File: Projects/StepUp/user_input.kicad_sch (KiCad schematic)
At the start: 1 part, among them U6 COM-09032

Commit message: feat(charge): Charge IC, USB ESD, sheet sections
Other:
- moved on the sheet: U6
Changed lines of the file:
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@@
 	(symbol
 		(lib_id "COM-09032:COM-09032")
-		(at 115.57 130.81 0)
+		(at 200.66 137.16 0)
 		(unit 1)
 		(exclude_from_sim no)
@@
 		(fields_autoplaced yes)
 		(property "Reference" "U6"
-			(at 124.46 130.8099 0)
+			(at 209.55 137.1599 0)
 			(effects
 				(font
@@
 		)
 		(property "Value" "COM-09032"
-			(at 124.46 133.3499 0)
+			(at 209.55 139.6999 0)
 			(effects
 				(font
@@
 		)
 		(property "Footprint" "joystick_footprints:XDCR_COM-09032"
-			(at 115.57 130.81 0)
+			(at 200.66 137.16 0)
 			(effects
 				(font
@@
 		)
 		(property "Datasheet" ""
-			(at 115.57 130.81 0)
+			(at 200.66 137.16 0)
 			(effects
 				(font
@@
 		)
 		(property "Description" ""
-			(at 115.57 130.81 0)
+			(at 200.66 137.16 0)
 			(effects
 				(font
@@
 		)
 		(property "MF" "SparkFun Electronics"
-			(at 115.57 130.81 0)
+			(at 200.66 137.16 0)
 			(effects
 				(font
@@
 		)
 		(property "MAXIMUM_PACKAGE_HEIGHT" "30.1mm"
-			(at 115.57 130.81 0)
+			(at 200.66 137.16 0)
 			(effects
 				(font
@@
 		)
 		(property "Package" "Package"
-			(at 115.57 130.81 0)
+			(at 200.66 137.16 0)
 			(effects
 				(font
@@
 		)
 		(property "Price" "None"
-			(at 115.57 130.81 0)
+			(at 200.66 137.16 0)
 			(effects
 				(font
@@
 		)
 		(property "Check_prices" "https://www.snapeda.com/parts/COM-09032/SparkFun+Electronics/view-part/?ref=eda"
-			(at 115.57 130.81 0)
+			(at 200.66 137.16 0)
 			(effects
 				(font
@@
 		)
 		(property "STANDARD" "Manufacturer Recommendations"
-			(at 115.57 130.81 0)
+			(at 200.66 137.16 0)
 			(effects
 				(font
@@
 		)
 		(property "PARTREV" "N/A"
-			(at 115.57 130.81 0)
+			(at 200.66 137.16 0)
 			(effects
 				(font
@@
 		)
 		(property "SnapEDA_Link" "https://www.snapeda.com/parts/COM-09032/SparkFun+Electronics/view-part/?ref=snap"
-			(at 115.57 130.81 0)
+			(at 200.66 137.16 0)
 			(effects
 				(font
@@
 		)
 		(property "MP" "COM-09032"
-			(at 115.57 130.81 0)
+			(at 200.66 137.16 0)
 			(effects
 				(font
@@
 		)
 		(property "Purchase-URL" "https://www.snapeda.com/api/url_track_click_mouser/?unipart_id=888157&manufacturer=SparkFun Electronics&part_name=COM-09032&search_term=joystick"
-			(at 115.57 130.81 0)
+			(at 200.66 137.16 0)
 			(effects
 				(font
@@
 		)
 		(property "Description_1" "\nJoystick, 2 - Axis Analog (Resistive) Output\n"
-			(at 115.57 130.81 0)
+			(at 200.66 137.16 0)
 			(effects
 				(font
@@
 		)
 		(property "Availability" "In Stock"
-			(at 115.57 130.81 0)
+			(at 200.66 137.16 0)
 			(effects
 				(font
@@
 		)
 		(property "MANUFACTURER" "SparkFun Electronics"
-			(at 115.57 130.81 0)
+			(at 200.66 137.16 0)
 			(effects
 				(font

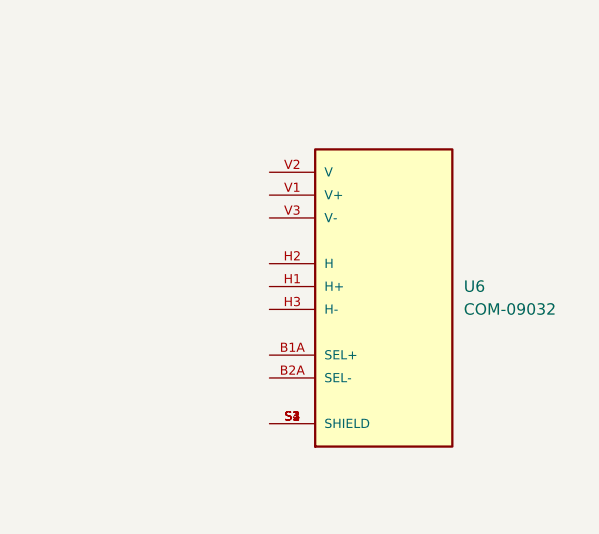
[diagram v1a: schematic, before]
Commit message: feat(power): Input stage updates
USB vs Vbat source selection using PMOS gate logic.
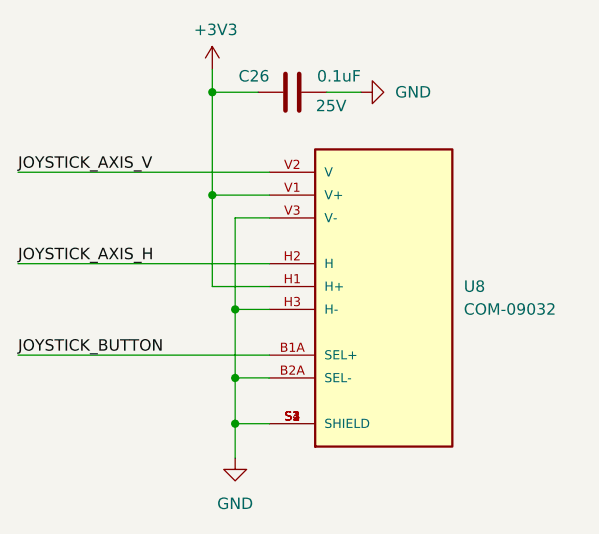
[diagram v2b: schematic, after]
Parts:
- added C26: 0.1uF, Capacitor_SMD:C_0603_1608Metric, symbol Device:C
- renumbered U6 to U8
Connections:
- net JOYSTICK_BUTTON: now reaches U8.B1A (SEL+)
- net GND: now reaches U8.B2A (SEL-)
- net GND: now also U8.H3 (H-), U8.S1 (SHIELD), U8.S2 (SHIELD), U8.S3 (SHIELD), U8.S4 (SHIELD), U8.V3 (V-), C26.2
- net +3V3: now reaches U8.H1 (H+)
- net +3V3: now also U8.V1 (V+), C26.1
- net JOYSTICK_AXIS_H: now reaches U8.H2 (H)
- net JOYSTICK_AXIS_V: now reaches U8.V2 (V)

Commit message: feat(stepup): Many additions
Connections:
- net JOYSTICK_AXIS_H renamed JOYSTSICK_AXIS_H
- net JOYSTICK_AXIS_V renamed JOYSTSICK_AXIS_V
- net JOYSTICK_BUTTON renamed JOYSTSICK_BUTTON
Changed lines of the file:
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@@
+		)
+	)
+	(global_label "JOYSTSICK_AXIS_H"
+		(shape input)
+		(at 160.02 134.62 180)
+		(fields_autoplaced yes)
+		(effects
+			(font
+				(size 1.27 1.27)
+				(color 255 255 194 1)
+			)
+			(justify right)
+		)
+		(property "Intersheetrefs" "${INTERSHEET_REFS}"
+			(at 139.7386 134.62 0)
+			(effects
+				(font
+					(size 1.27 1.27)
+				)
+				(justify right)
+				(hide yes)
+			)
+		)
+	)
+	(global_label "JOYSTSICK_AXIS_V"
+		(shape input)
+		(at 160.02 124.46 180)
+		(fields_autoplaced yes)
+		(effects
+			(font
+				(size 1.27 1.27)
+				(color 255 255 194 1)
+			)
+			(justify right)
+		)
+		(property "Intersheetrefs" "${INTERSHEET_REFS}"
+			(at 139.9805 124.46 0)
+			(effects
+				(font
+					(size 1.27 1.27)
+				)
+				(justify right)
+				(hide yes)
+			)
+		)
+	)
+	(global_label "JOYSTSICK_BUTTON"
+		(shape input)
+		(at 160.02 144.78 180)
+		(fields_autoplaced yes)
+		(effects
+			(font
+				(size 1.27 1.27)
+				(color 255 255 194 1)
+			)
+			(justify right)
+		)
+		(property "Intersheetrefs" "${INTERSHEET_REFS}"
+			(at 138.9524 144.78 0)
+			(effects
+				(font
+					(size 1.27 1.27)
+				)
+				(justify right)
+				(hide yes)
+			)
 		)
 	)
@@
 				(path "/e0cca1c7-c263-49eb-8c40-74000ebe5285/62dd6998-8b69-42c0-9c2f-b18953d44bc4"
 					(reference "C26")
+					(unit 1)
+				)
+				(path "/e0cca1c7-c263-49eb-8c40-74000ebe5285/b287fd2a-b2a9-45b4-81d1-0975d80d8cfc"
+					(reference "C28")
 					(unit 1)
 				)
@@
 					(unit 1)
 				)
+				(path "/e0cca1c7-c263-49eb-8c40-74000ebe5285/b287fd2a-b2a9-45b4-81d1-0975d80d8cfc"
+					(reference "U9")
+					(unit 1)
+				)
 			)
 		)
@@
 				(path "/e0cca1c7-c263-49eb-8c40-74000ebe5285/62dd6998-8b69-42c0-9c2f-b18953d44bc4"
 					(reference "#PWR038")
+					(unit 1)
+				)
+				(path "/e0cca1c7-c263-49eb-8c40-74000ebe5285/b287fd2a-b2a9-45b4-81d1-0975d80d8cfc"
+					(reference "#PWR056")
 					(unit 1)
 				)
@@
 					(unit 1)
 				)
+				(path "/e0cca1c7-c263-49eb-8c40-74000ebe5285/b287fd2a-b2a9-45b4-81d1-0975d80d8cfc"
+					(reference "#PWR058")
+					(unit 1)
+				)
 			)
 		)
@@
 					(unit 1)
 				)
+				(path "/e0cca1c7-c263-49eb-8c40-74000ebe5285/b287fd2a-b2a9-45b4-81d1-0975d80d8cfc"
+					(reference "#PWR057")
+					(unit 1)
+				)

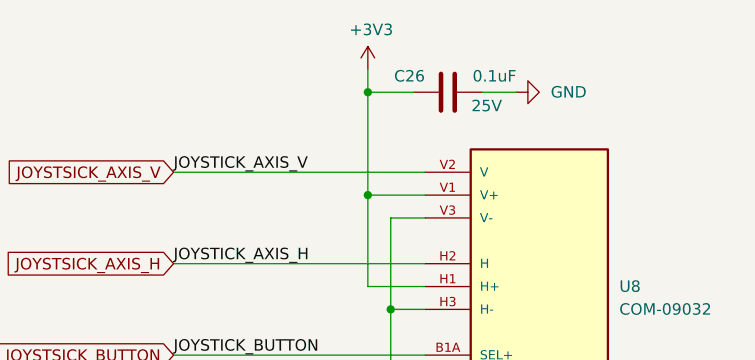
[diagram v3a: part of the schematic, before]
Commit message: feat(stepup): Schematic + PCB updates
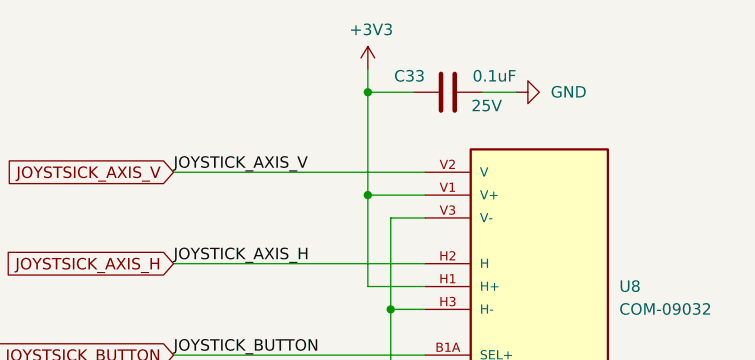
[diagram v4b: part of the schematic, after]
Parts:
- renumbered C26 to C33
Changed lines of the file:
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@@
 		(on_board yes)
 		(dnp no)
-		(property "Reference" "C26"
+		(property "Reference" "C33"
 			(at 187.96 113.792 90)
 			(effects
@@
 			(project "StepUp"
 				(path "/e0cca1c7-c263-49eb-8c40-74000ebe5285/62dd6998-8b69-42c0-9c2f-b18953d44bc4"
-					(reference "C26")
-					(unit 1)
-				)
-				(path "/e0cca1c7-c263-49eb-8c40-74000ebe5285/b287fd2a-b2a9-45b4-81d1-0975d80d8cfc"
-					(reference "C28")
+					(reference "C33")
 					(unit 1)
 				)
@@
 					(unit 1)
 				)
-				(path "/e0cca1c7-c263-49eb-8c40-74000ebe5285/b287fd2a-b2a9-45b4-81d1-0975d80d8cfc"
-					(reference "U9")
-					(unit 1)
-				)
 			)
 		)
@@
 		(on_board yes)
 		(dnp no)
-		(property "Reference" "#PWR038"
+		(property "Reference" "#PWR073"
 			(at 181.61 116.84 0)
 			(effects
@@
 			(project "StepUp"
 				(path "/e0cca1c7-c263-49eb-8c40-74000ebe5285/62dd6998-8b69-42c0-9c2f-b18953d44bc4"
-					(reference "#PWR038")
-					(unit 1)
-				)
-				(path "/e0cca1c7-c263-49eb-8c40-74000ebe5285/b287fd2a-b2a9-45b4-81d1-0975d80d8cfc"
-					(reference "#PWR056")
+					(reference "#PWR073")
 					(unit 1)
 				)
@@
 		(dnp no)
 		(fields_autoplaced yes)
-		(property "Reference" "#PWR040"
+		(property "Reference" "#PWR075"
 			(at 204.47 115.57 0)
 			(effects
@@
 			(project "StepUp"
 				(path "/e0cca1c7-c263-49eb-8c40-74000ebe5285/62dd6998-8b69-42c0-9c2f-b18953d44bc4"
-					(reference "#PWR040")
-					(unit 1)
-				)
-				(path "/e0cca1c7-c263-49eb-8c40-74000ebe5285/b287fd2a-b2a9-45b4-81d1-0975d80d8cfc"
-					(reference "#PWR058")
+					(reference "#PWR075")
 					(unit 1)
 				)
@@
 		(dnp no)
 		(fields_autoplaced yes)
-		(property "Reference" "#PWR039"
+		(property "Reference" "#PWR074"
 			(at 184.15 162.56 0)
 			(effects
@@
 			(project "StepUp"
 				(path "/e0cca1c7-c263-49eb-8c40-74000ebe5285/62dd6998-8b69-42c0-9c2f-b18953d44bc4"
-					(reference "#PWR039")
+					(reference "#PWR074")
 					(unit 1)
 				)
-				(path "/e0cca1c7-c263-49eb-8c40-74000ebe5285/b287fd2a-b2a9-45b4-81d1-0975d80d8cfc"
-					(reference "#PWR057")
-					(unit 1)
-				)

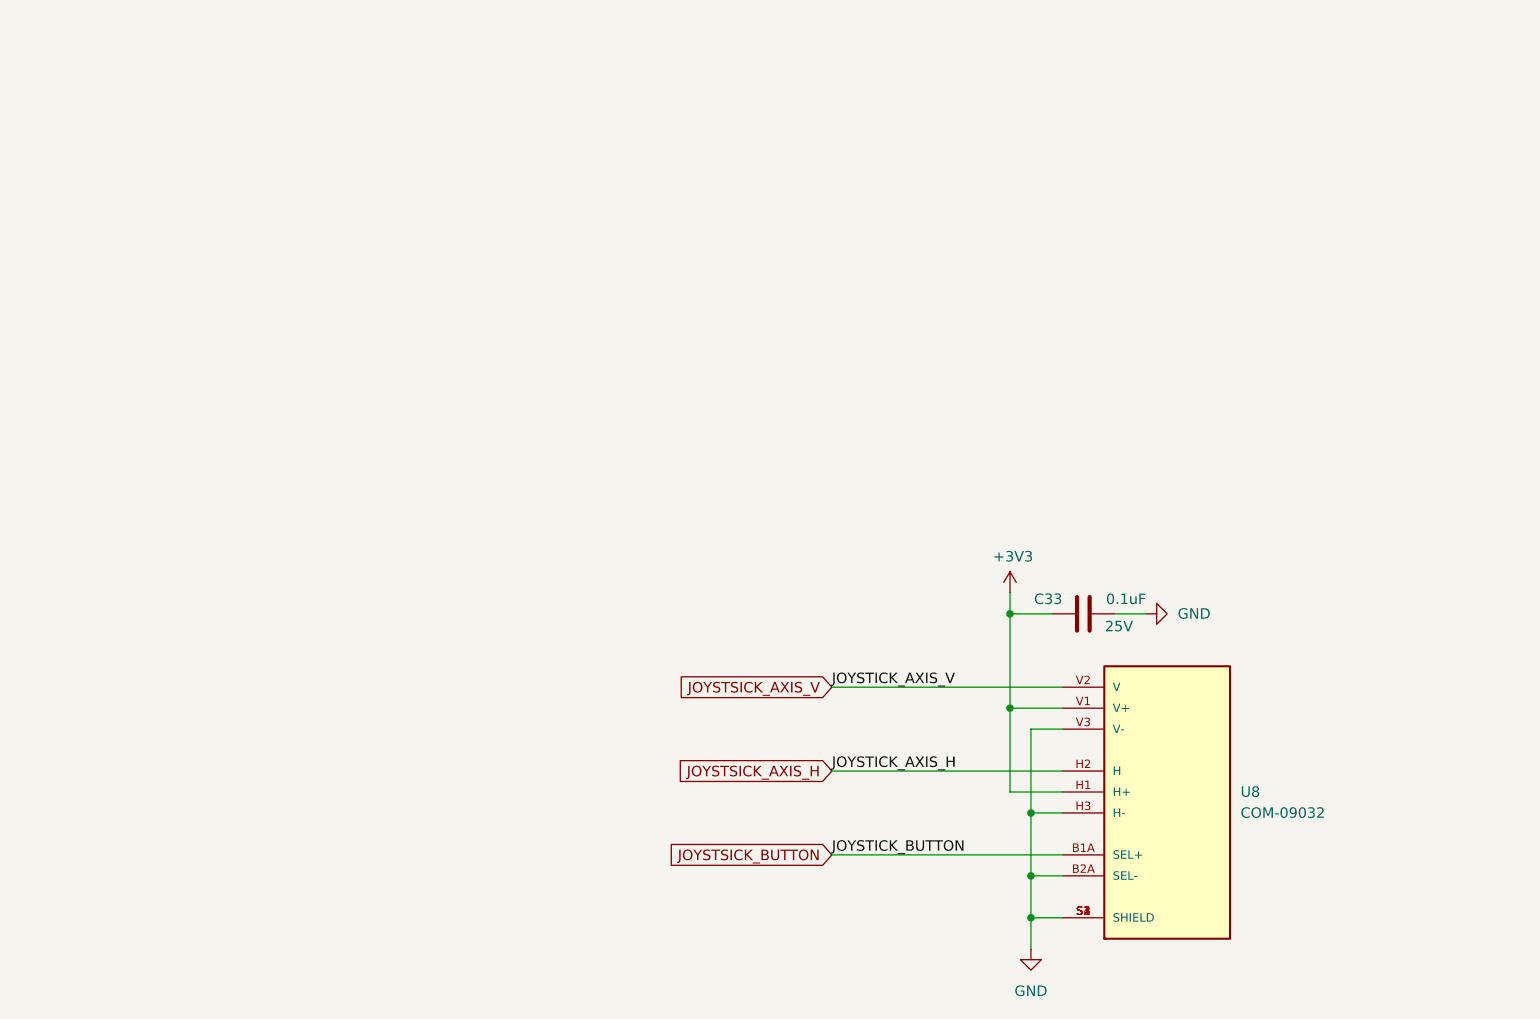
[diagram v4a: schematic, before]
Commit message: feat(schematic): Ready for layout
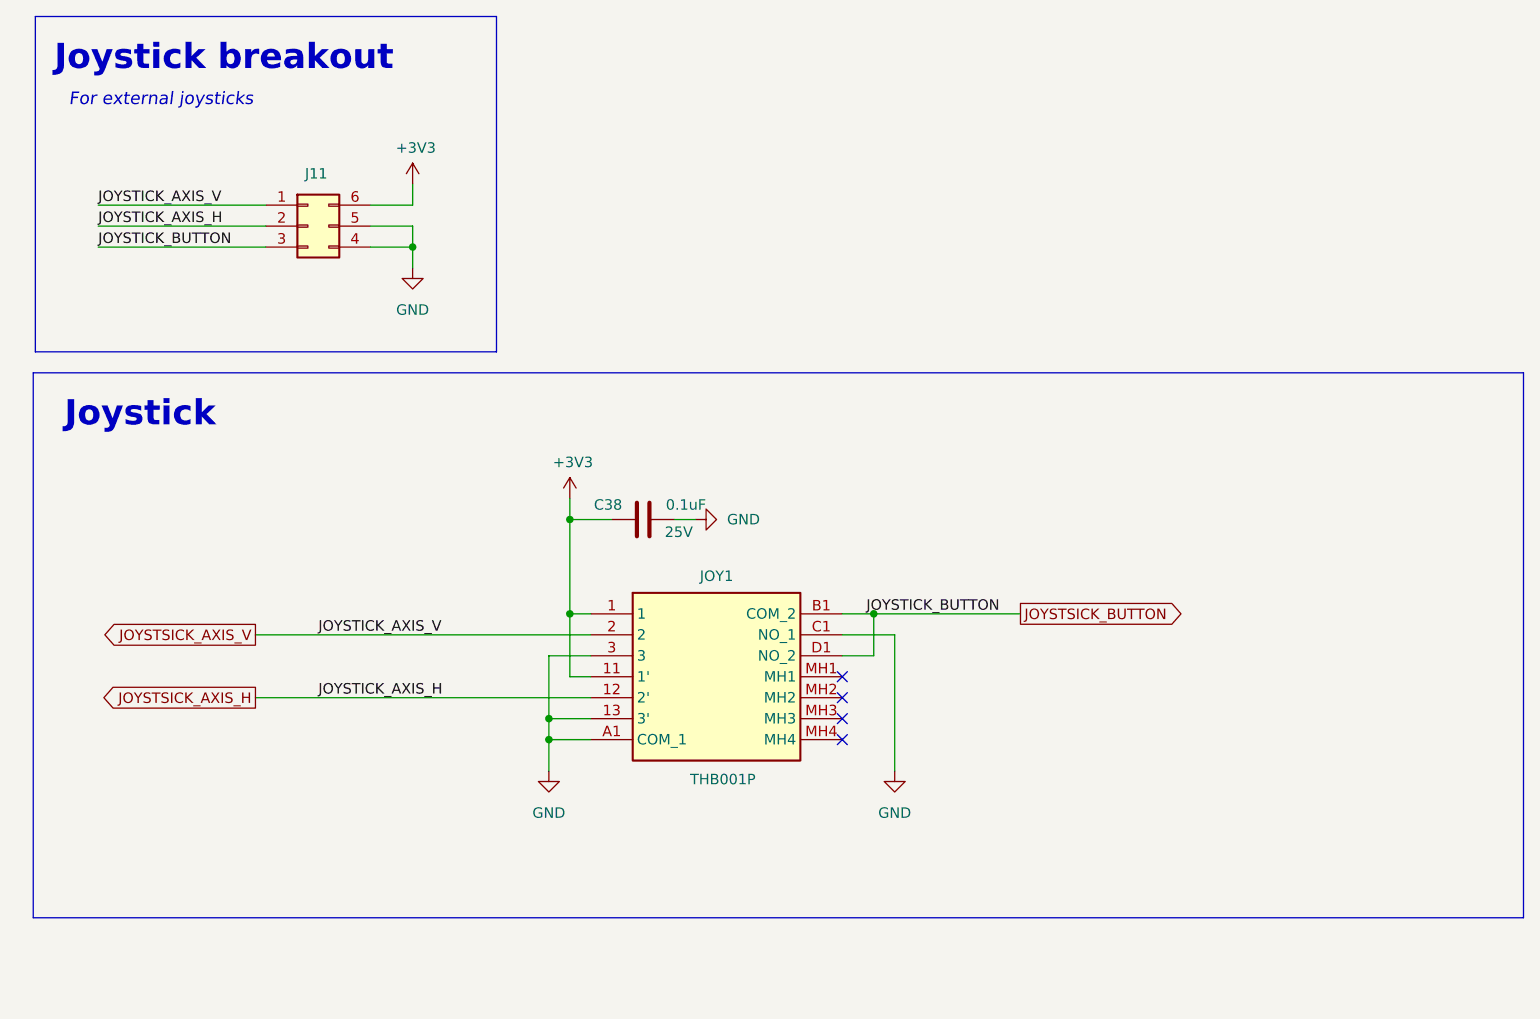
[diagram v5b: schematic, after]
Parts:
- removed C33: 0.1uF, Capacitor_SMD:C_0603_1608Metric, symbol Device:C
- removed U8: COM-09032, joystick_footprints:XDCR_COM-09032, symbol COM-09032:COM-09032
- added C38: 0.1uF, Capacitor_SMD:C_0603_1608Metric, symbol Device:C
- added J11: Conn_02x03_Counter_Clockwise, Connector_PinHeader_2.54mm:PinHeader_2x03_P2.54mm_Vertical, symbol Connector_Generic:Conn_02x03_Counter_Clockwise
- added JOY1: THB001P, Samacsys:THB001P, symbol Samacsys:THB001P
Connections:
- net +3V3: now also C38.1, J11.6 (Pin_6), JOY1.1, JOY1.11 (1')
- net GND: now also C38.2, J11.4 (Pin_4), J11.5 (Pin_5), JOY1.13 (3'), JOY1.3, JOY1.A1 (COM_1), JOY1.C1 (NO_1)
- net JOYSTSICK_AXIS_H: now also J11.2 (Pin_2), JOY1.12 (2')
- net JOYSTSICK_AXIS_V: now also J11.1 (Pin_1), JOY1.2
- net JOYSTSICK_BUTTON: now also J11.3 (Pin_3), JOY1.B1 (COM_2), JOY1.D1 (NO_2)
- no-connect marks 0 -> 4
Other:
- note added: "For external joysticks"
- note added: "Joystick"
- note added: "Joystick breakout"
- company: (none) -> Samio
- title: (none) -> User Input

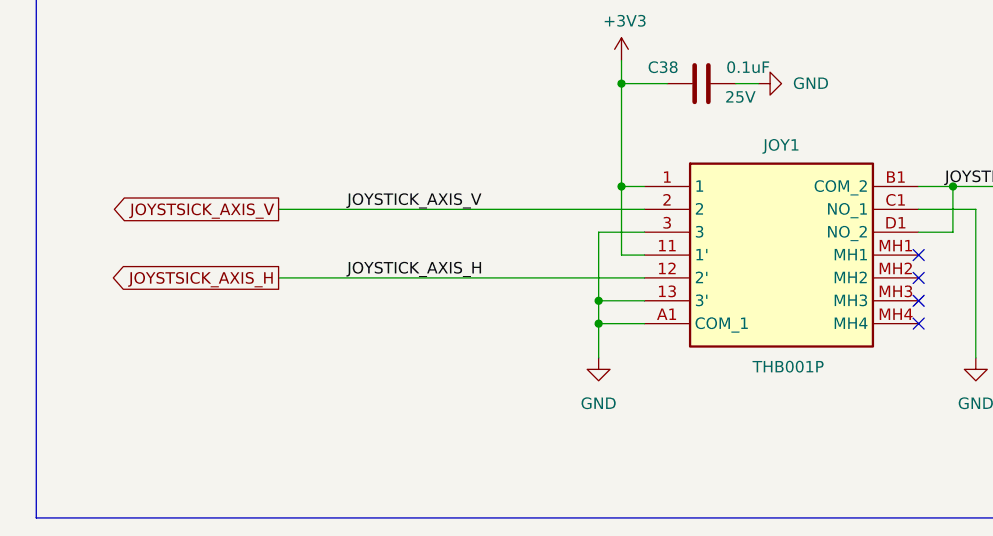
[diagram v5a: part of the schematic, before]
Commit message: chore(pins): MCU_BOOST_EN to MCU, fixed errors
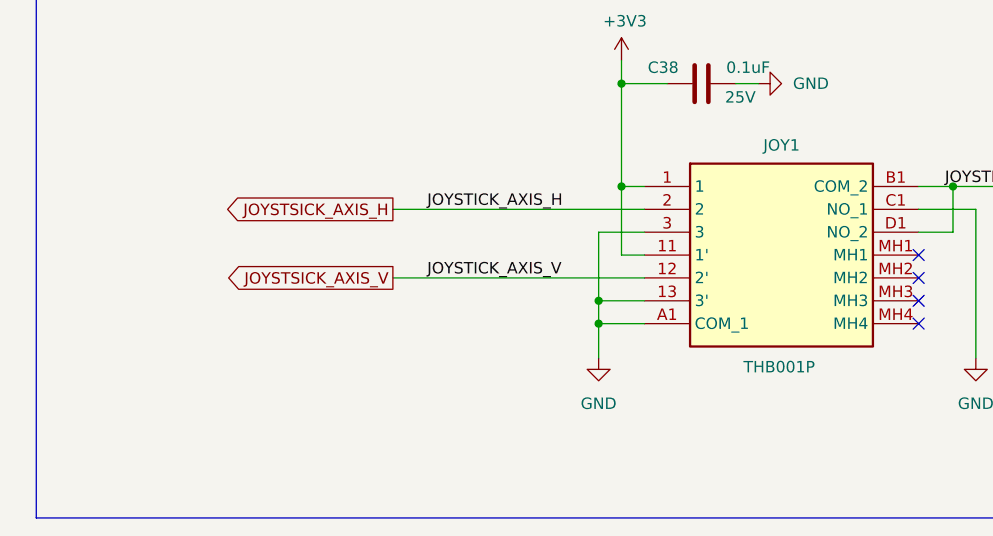
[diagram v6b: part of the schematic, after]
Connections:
- net JOYSTSICK_AXIS_H: now also JOY1.2; no longer JOY1.12 (2')
- net JOYSTSICK_AXIS_V: now also JOY1.12 (2'); no longer JOY1.2
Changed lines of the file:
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@@
 	(wire
 		(pts
-			(xy 90.17 118.11) (xy 130.81 118.11)
+			(xy 102.87 118.11) (xy 130.81 118.11)
 		)
 		(stroke
@@
 	(wire
 		(pts
-			(xy 90.17 125.73) (xy 130.81 125.73)
+			(xy 102.87 125.73) (xy 130.81 125.73)
 		)
 		(stroke
@@
 		)
 	)
-	(label "JOYSTICK_AXIS_H"
-		(at 97.79 125.73 0)
+	(label "JOYSTICK_AXIS_V"
+		(at 106.68 125.73 0)
 		(fields_autoplaced yes)
 		(effects
@@
 		)
 	)
-	(label "JOYSTICK_AXIS_V"
-		(at 97.79 118.11 0)
-		(fields_autoplaced yes)
-		(effects
-			(font
-				(size 1.27 1.27)
-			)
-			(justify left bottom)
-		)
-	)
 	(label "JOYSTICK_AXIS_H"
 		(at 71.12 68.58 0)
@@
 		)
 	)
+	(label "JOYSTICK_AXIS_H"
+		(at 106.68 118.11 0)
+		(fields_autoplaced yes)
+		(effects
+			(font
+				(size 1.27 1.27)
+			)
+			(justify left bottom)
+		)
+	)
 	(label "JOYSTICK_BUTTON"
 		(at 71.12 71.12 0)
@@
 			)
 			(justify left bottom)
+		)
+	)
+	(global_label "JOYSTSICK_AXIS_H"
+		(shape output)
+		(at 102.87 118.11 180)
+		(fields_autoplaced yes)
+		(effects
+			(font
+				(size 1.27 1.27)
+				(color 255 255 194 1)
+			)
+			(justify right)
+		)
+		(property "Intersheetrefs" "${INTERSHEET_REFS}"
+			(at 82.5886 118.11 0)
+			(effects
+				(font
+					(size 1.27 1.27)
+				)
+				(justify right)
+				(hide yes)
+			)
 		)
 	)
@@
 		)
 	)
-	(global_label "JOYSTSICK_AXIS_H"
+	(global_label "JOYSTSICK_AXIS_V"
 		(shape output)
-		(at 90.17 125.73 180)
+		(at 102.87 125.73 180)
 		(fields_autoplaced yes)
 		(effects
@@
 		)
 		(property "Intersheetrefs" "${INTERSHEET_REFS}"
-			(at 69.8886 125.73 0)
-			(effects
-				(font
-					(size 1.27 1.27)
-				)
-				(justify right)
-				(hide yes)
-			)
-		)
-	)
-	(global_label "JOYSTSICK_AXIS_V"
-		(shape output)
-		(at 90.17 118.11 180)
-		(fields_autoplaced yes)
-		(effects
-			(font
-				(size 1.27 1.27)
-				(color 255 255 194 1)
-			)
-			(justify right)
-		)
-		(property "Intersheetrefs" "${INTERSHEET_REFS}"
-			(at 70.1305 118.11 0)
+			(at 82.8305 125.73 0)
 			(effects
 				(font
@@
 		)
 		(property "Value" "THB001P"
-			(at 146.812 135.636 0)
+			(at 145.796 135.636 0)
 			(effects
 				(font
@@
 			)
 		)
-		(property "Description" ""
+		(property "Description" "Power symbol creates a global label with name \"+3V3\""
 			(at 109.22 63.5 0)
 			(effects
@@
 			)
 		)
-		(property "Description" ""
+		(property "Description" "Power symbol creates a global label with name \"+3V3\""
 			(at 128.27 101.6 0)
 			(effects
